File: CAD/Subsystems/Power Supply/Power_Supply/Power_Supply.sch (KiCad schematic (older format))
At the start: 14 parts, among them Q1 BS170, Q2 2N2222, SW1 SW_DPST

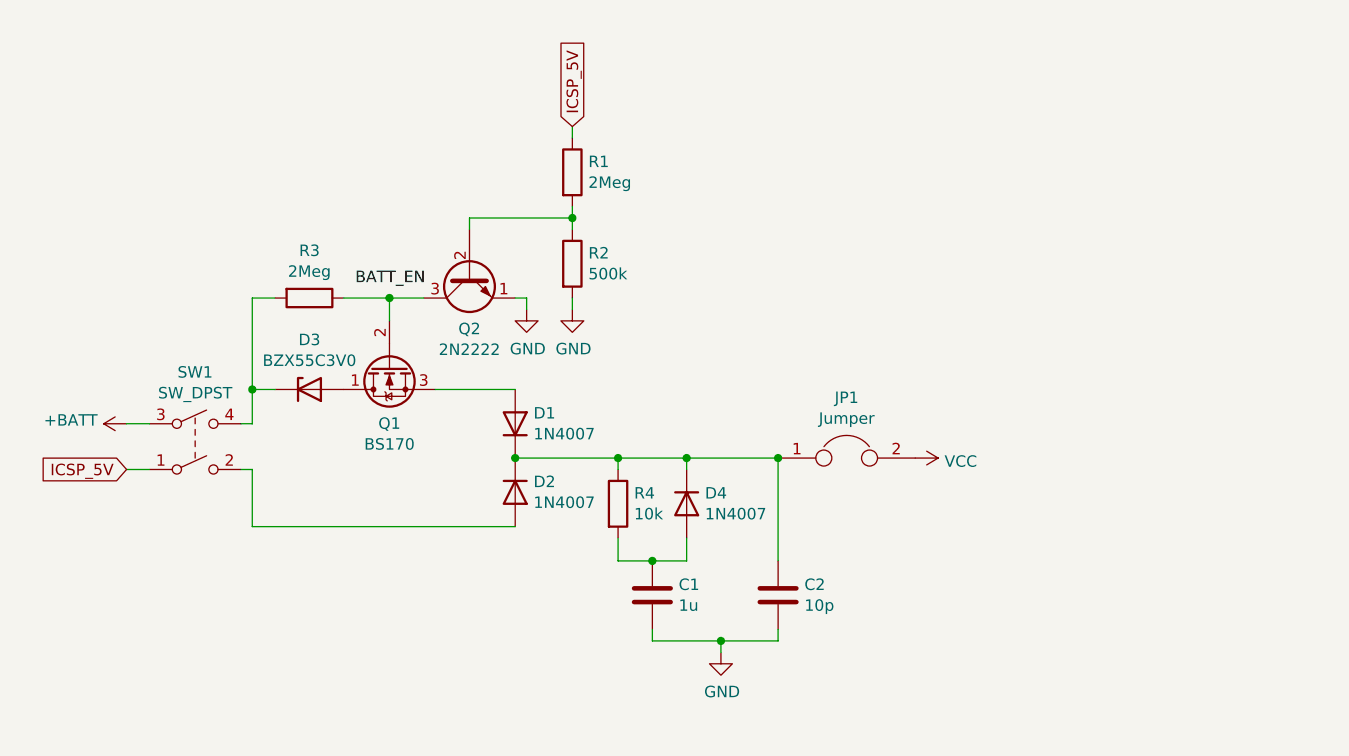
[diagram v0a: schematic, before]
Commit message: Voltage regulator redesign
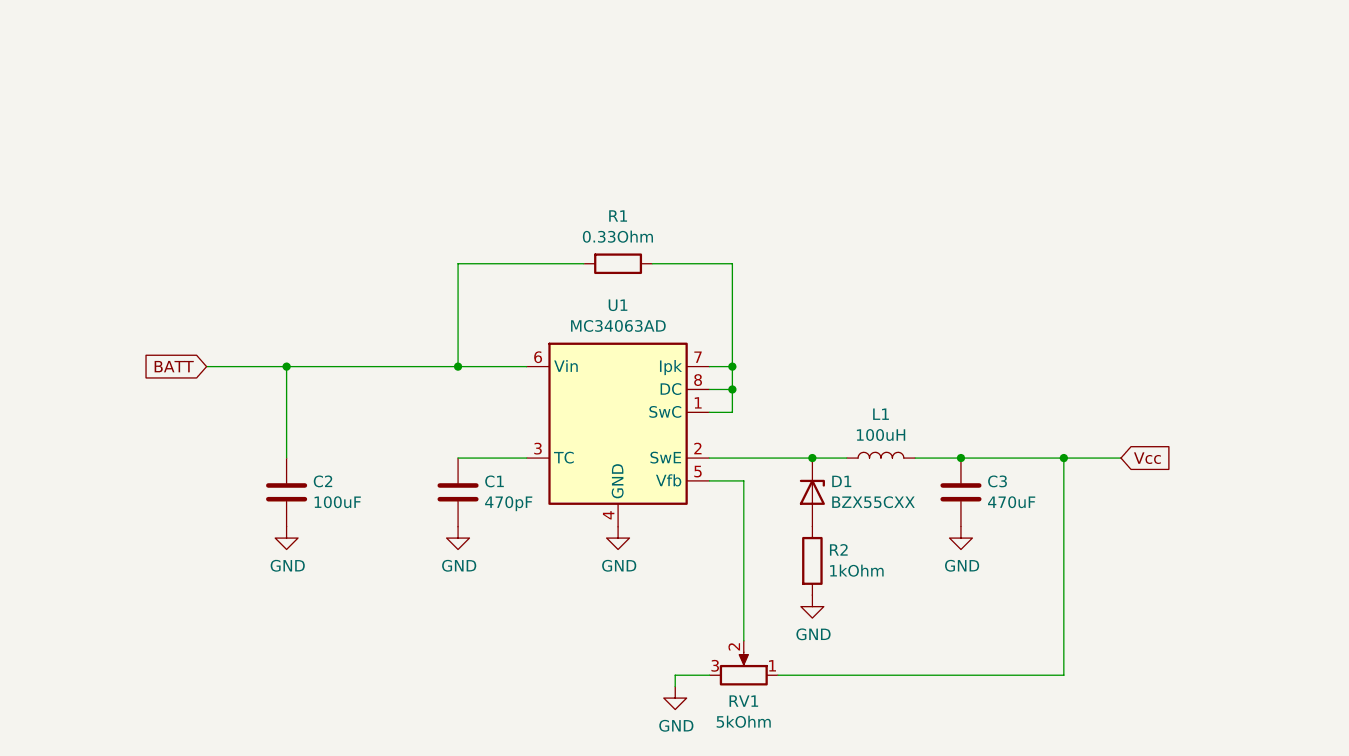
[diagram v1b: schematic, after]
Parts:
- removed D1, D2, D4: 1N4007, Diode_THT:D_DO-41_SOD81_P10.16mm_Horizontal, symbol Diode:1N4007
- removed D3: BZX55C3V0, DO-35, symbol Diode:BZX55C3V0
- removed JP1: Jumper, symbol Device:Jumper
- removed Q1: BS170, Package_TO_SOT_THT:TO-92_Inline, symbol Transistor_FET:BS170
- removed Q2: 2N2222, TO-92, symbol Transistor_BJT:2N2222
- removed R3: 2Meg, symbol Device:R
- removed R4: 10k, symbol Device:R
- removed SW1: SW_DPST, symbol Switch:SW_DPST
- added C3: 470uF, symbol Device:C
- added D1: BZX55CXX, DO-35, symbol Diode:BZX55C3V0
- added L1: 100uH, symbol Device:L
- added RV1: 5kOhm, symbol Device:R_POT
- added U1: MC34063AD, Package_SO:SOIC-8_3.9x4.9mm_P1.27mm, symbol Regulator_Switching:MC34063AD
- C1: value 1u -> 470pF
- C2: value 10p -> 100uF
- R1: value 2Meg -> 0.33Ohm
- R2: value 500k -> 1kOhm
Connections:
- net GND: now also C3.2, RV1.3, U1.4 (GND)
- net BATT: now reaches C2.1
- net BATT: now also R1.2, U1.6 (Vin)
- net at R2.1: now also D1.2 (A); no longer R1.2
- net at C1.1: now also U1.3 (TC)
- net ICSP_5V: no longer names the net of R1.1
- net ICSP_5V: now also U1.1 (SwC), U1.7 (Ipk), U1.8 (DC)
- new net: D1.1 (K), L1.1, U1.2 (SwE)
- new net: RV1.2, U1.5 (Vfb)
- new net Vcc: C3.1, L1.2, RV1.1

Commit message: Added switch and calibration jumper
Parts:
- added JP1: Jumper_NC_Dual, symbol Device:Jumper_NC_Dual
- added R3: 150, symbol Device:R
- added SW1: SW_SPST, symbol Switch:SW_SPST
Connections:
- net BATT: now also SW1.1 (A); no longer C2.1, R1.2, U1.6 (Vin)
- net GND: now also R3.2
- net Vcc: now also JP1.1; no longer C3.1, L1.2, RV1.1
- new net: C2.1, R1.2, SW1.2 (B), U1.6 (Vin)
- new net: C3.1, JP1.2, L1.2, RV1.1
- new net: JP1.3, R3.1
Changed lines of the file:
@@
 Wire Wire Line
 	4500 3400 4500 3800
-Wire Wire Line
-	4500 3400 4150 3400
-Connection ~ 4500 3400
-Text GLabel 4150 3400 0    50   Input ~ 0
+Text GLabel 3950 3400 0    50   Input ~ 0
 BATT
 $Comp
@@
 Wire Wire Line
 	6200 4750 6200 4800
-Text GLabel 8150 3800 2    50   Input ~ 0
+Text GLabel 8800 3550 2    50   Input ~ 0
 Vcc
-Wire Wire Line
-	7900 3800 8150 3800
+$Comp
+L Switch:SW_SPST SW1
+U 1 1 618B42B0
+P 4250 3400
+F 0 "SW1" H 4250 3635 50  0000 C CNN
+F 1 "SW_SPST" H 4250 3544 50  0000 C CNN
+F 2 "" H 4250 3400 50  0001 C CNN
+F 3 "~" H 4250 3400 50  0001 C CNN
+	1    4250 3400
+	1    0    0    -1
+$EndComp
+Wire Wire Line
+	3950 3400 4050 3400
+Wire Wire Line
+	4450 3400 4500 3400
+Connection ~ 4500 3400
+$Comp
+L Device:Jumper_NC_Dual JP1
+U 1 1 618B7794
+P 8100 3800
+F 0 "JP1" V 8054 3902 50  0000 L CNN
+F 1 "Jumper_NC_Dual" V 8145 3902 50  0000 L CNN
+F 2 "" H 8100 3800 50  0001 C CNN
+F 3 "~" H 8100 3800 50  0001 C CNN
+	1    8100 3800
+	0    1    1    0
+$EndComp
+$Comp
+L Device:R R3
+U 1 1 618B94E7
+P 8100 4300
+F 0 "R3" H 8170 4346 50  0000 L CNN
+F 1 "150" H 8170 4255 50  0000 L CNN
+F 2 "" V 8030 4300 50  0001 C CNN
+F 3 "~" H 8100 4300 50  0001 C CNN
+	1    8100 4300
+	1    0    0    -1
+$EndComp
+$Comp
+L power:GND #PWR?
+U 1 1 618BA902
+P 8100 4450
+F 0 "#PWR?" H 8100 4200 50  0001 C CNN
+F 1 "GND" H 8105 4277 50  0000 C CNN
+F 2 "" H 8100 4450 50  0001 C CNN
+F 3 "" H 8100 4450 50  0001 C CNN
+	1    8100 4450
+	1    0    0    -1
+$EndComp
+Wire Wire Line
+	7900 3800 8000 3800
 Connection ~ 7900 3800
+Wire Wire Line
+	8100 3550 8800 3550
+Wire Wire Line
+	8100 4050 8100 4150
 $EndSCHEMATC
